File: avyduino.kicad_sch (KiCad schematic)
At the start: 4 parts, among them J1 Power, J2 Digital/PWM, J3 Analog, J4 Digital/PWM

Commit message: make schematic
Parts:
- added C1, C10, C11, C12, C13, C14, C2, C3, C6, C9: 100nF, symbol Device:C
- added C4, C5, C7, C8: 22pF, symbol Device:C
- added D1: D, symbol Device:D
- added FB1: 10uH, symbol Device:FerriteBead
- added J5: USB_C_Receptacle_USB2.0_14P, symbol Connector:USB_C_Receptacle_USB2.0_14P
- added Q1: AO3401A, Package_TO_SOT_SMD:SOT-23, symbol Transistor_FET:AO3401A
- added R1, R5, R6: 10k, symbol Device:R
- added R2: 1m, symbol Device:R
- added R3, R4: 5.1k, symbol Device:R
- added U1: ATmega328P-P, Package_DIP:DIP-28_W7.62mm_Socket_LongPads, symbol MCU_Microchip_ATmega:ATmega328P-P
- added U2: CH340G, Package_SO:SOIC-16_3.9x9.9mm_P1.27mm, symbol Interface_USB:CH340G
- added U3: LM2931AZ-5.0_TO92, Package_TO_SOT_THT:TO-92_Inline, symbol Regulator_Linear:LM2931AZ-5.0_TO92
- added U4: MCP1700x-330xxTT, Package_TO_SOT_SMD:SOT-23, symbol Regulator_Linear:MCP1700x-330xxTT
- added U5: LM358, symbol Amplifier_Operational:LM358
- added Y1: 12MHz, symbol Device:Crystal
- added Y2: 16MHz, symbol Device:Crystal
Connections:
- net IOREF is gone; now on net +5V: J1.2 (Pin_2)
- net *10: now also U1.16 (PB2)
- net *11: now also U1.17 (PB3)
- net *3: now also U1.5 (PD3)
- net *5: now also U1.11 (PD5)
- net *6: now also U1.12 (PD6)
- net *9: now also U1.15 (PB1)
- net +3V3: now also C13.2, U4.2 (VO)
- net +5V: now also C1.1, C11.2, C14.2, FB1.1, Q1.3 (D), R1.1, U1.7 (VCC), U2.16 (VCC), U3.1 (VO), U5.8 (V+)
- net 12: now also U1.18 (PB4)
- net 13: now also U1.19 (PB5)
- net 2: now also U1.4 (PD2)
- net 4: now also U1.6 (PD4)
- net 7: now also U1.13 (PD7)
- net 8: now also U1.14 (PB0)
- net A0: now also U1.23 (PC0)
- net A1: now also U1.24 (PC1)
- net A2: now also U1.25 (PC2)
- net A3: now also U1.26 (PC3)
- net AREF: now also C3.1, U1.21 (AREF)
- net GND: now also C1.2, C10.1, C11.1, C12.1, C13.1, C14.1, C2.2, C3.2, C4.2, C5.2, C7.2, C8.2, C9.2, D1.1 (K), J5.A1 (GND), J5.A12 (GND), J5.B1 (GND), J5.B12 (GND), J5.SH (SHIELD), R3.2, R4.2, R6.2, U1.22 (GND), U1.8 (GND), U2.1 (GND), U3.2 (GND), U4.1 (GND), U5.4 (V-)
- net RX/0: now also U1.2 (PD0), U2.2 (TXD)
- net SCL/A5: now also U1.28 (PC5)
- net SDA/A4: now also U1.27 (PC4)
- net TX/1: now also U1.3 (PD1), U2.3 (RXD)
- net VCC: now also C10.2, C12.2, R5.1, U3.3 (VI), U4.3 (VI)
- net ~{RESET}: now also C6.1, U1.1 (~{RESET}/PC6)
- new net: Q1.1 (G), U5.1
- new net: R5.2, R6.1, U5.2 (-)
- new net: J5.A5 (CC1), R3.1
- new net: C4.1, U2.7 (XI), Y1.1
- new net: C5.1, U2.8 (XO), Y1.2
- new net: C9.1, U2.4 (V3)
- new net: C2.1, FB1.2, U1.20 (AVCC)
- new net: D1.2 (A), R1.2
- new net: J5.B5 (CC2), R4.1
- new net DTR: C6.2, U2.13 (~{DTR})
- new net UD+: J5.A6 (D+), J5.B6 (D+), U2.5 (UD+)
- new net UD-: J5.A7 (D-), J5.B7 (D-), U2.6 (UD-)
- new net VBUS: J5.A4 (VBUS), J5.A9 (VBUS), J5.B4 (VBUS), J5.B9 (VBUS), Q1.2 (S), U5.3 (+)
- new net XTAL1: C8.1, R2.2, U1.9 (XTAL1/PB6), Y2.2
- new net XTAL2: C7.1, R2.1, U1.10 (XTAL2/PB7), Y2.1
- no-connect marks 1 -> 6
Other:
- note added: "3v3 + 5v LDOs"
- note added: "MOSFET for deciding power source"
- note added: "Oscillator for ATmega"
- note added: "Pin Headers"
- note added: "USB to UART"
- note added: "USBC"

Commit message: do layout
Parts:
- removed FB1: 10uH, symbol Device:FerriteBead
- C1, C10, C11, C12, C13, C14, C2, C3, C4, C5, C6, C7, C8, C9: footprint (none) -> Capacitor_SMD:C_0805_2012Metric
- D1: footprint (none) -> Diode_THT:D_DO-35_SOD27_P10.16mm_Horizontal
- J5: footprint (none) -> Connector_USB:USB_C_Receptacle_GCT_USB4105-xx-A_16P_TopMnt_Horizontal
- Q1: MPN (none) -> AO3401A
- R1, R2, R3, R4, R5, R6: footprint (none) -> Resistor_SMD:R_0805_2012Metric
- U1: MPN (none) -> ATmega328P-P
- U2: MPN (none) -> CH340G
- U3: MPN (none) -> LM2931AZ-5.0_TO92
- U4: MPN (none) -> MCP1700x-330xxTT
- U5: footprint (none) -> Package_DIP:DIP-8_W7.62mm_Socket_LongPads; MPN (none) -> LM358
- Y1, Y2: footprint (none) -> Crystal:Crystal_HC49-U_Vertical
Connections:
- net +5V: now also C2.1, U1.20 (AVCC)

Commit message: added icsp header
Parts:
- added J6: ICSP Header, Connector_PinHeader_2.54mm:PinHeader_2x03_P2.54mm_Vertical, symbol Connector_Generic:Conn_02x03_Odd_Even
- added R7: R, Resistor_SMD:R_0805_2012Metric_Pad1.20x1.40mm_HandSolder, symbol Device:R
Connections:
- net *11: now also J6.4 (Pin_4)
- net +5V: now also J6.2 (Pin_2), R7.1
- net 12: now also J6.1 (Pin_1)
- net 13: now also J6.3 (Pin_3)
- net GND: now also J6.6 (Pin_6)
- net ~{RESET}: now also J6.5 (Pin_5), R7.2
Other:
- note added: "ICSP Header"
- moved on the sheet: C1, C2, C3, C6, U1

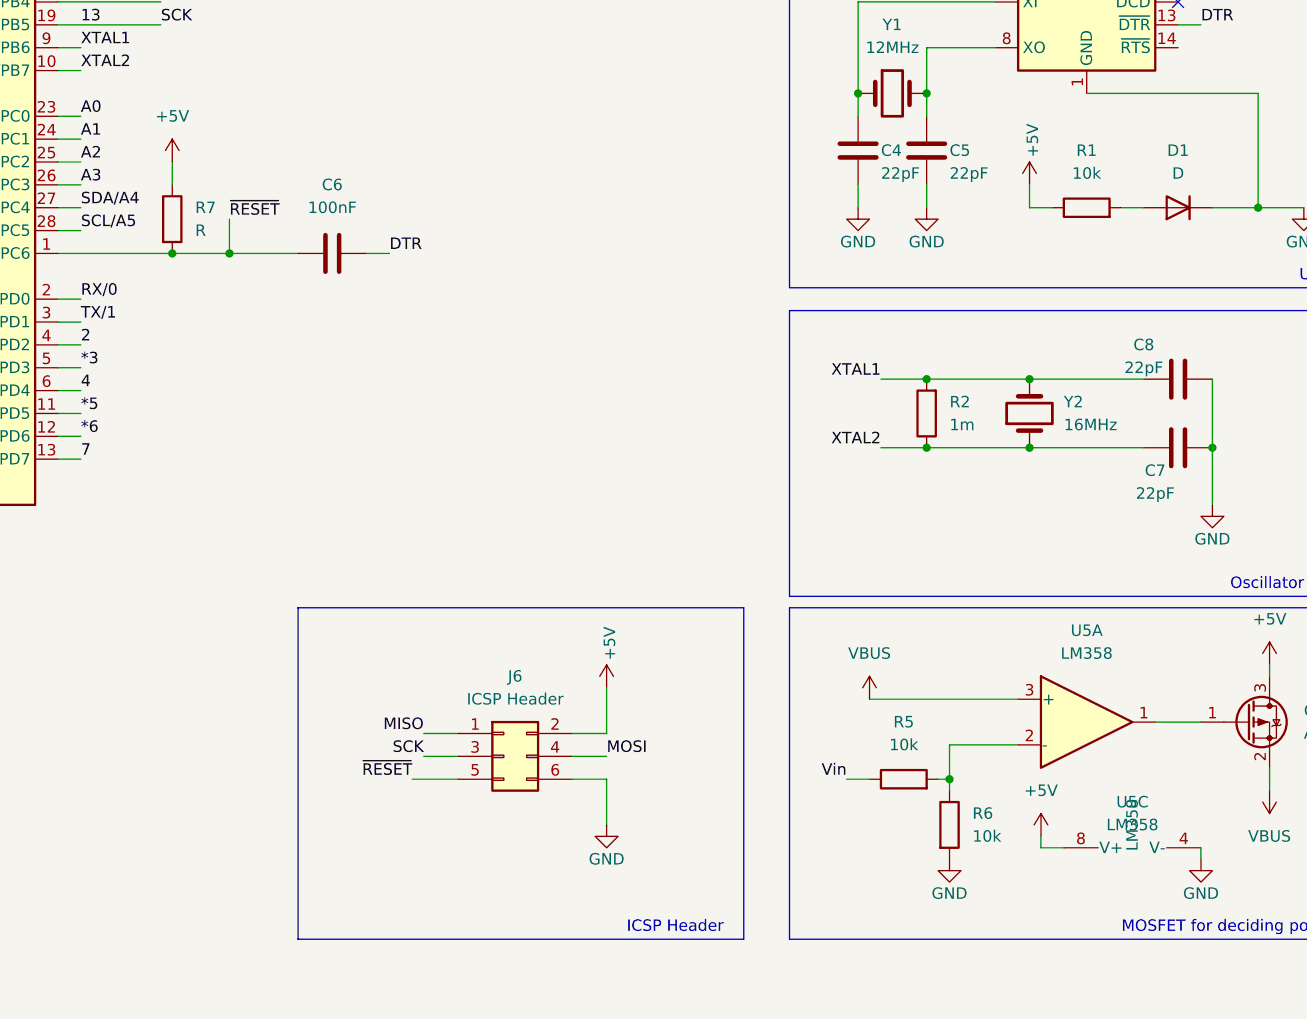
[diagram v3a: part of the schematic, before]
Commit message: routed ICSP header
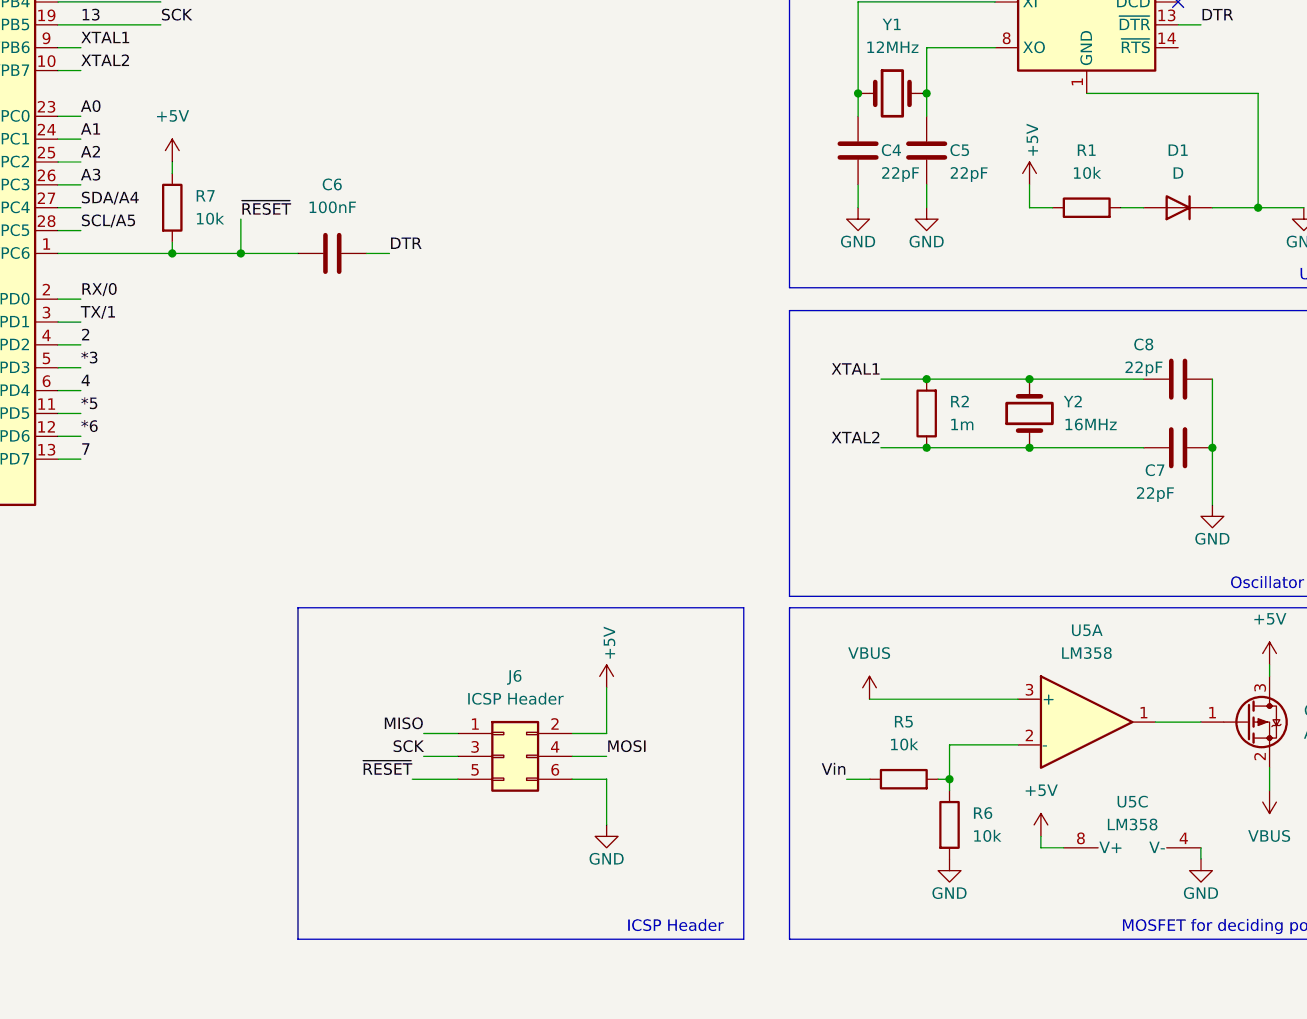
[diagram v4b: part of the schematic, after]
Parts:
- R7: value R -> 10k
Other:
- moved on the sheet: R7
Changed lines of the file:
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@@
 	)
 	(junction
-		(at 148.59 87.63)
-		(diameter 0)
-		(color 0 0 0 0)
-	)
-	(junction
 		(at 226.06 69.85)
 		(diameter 0)
@@
 	)
 	(junction
+		(at 149.86 87.63)
+		(diameter 0)
+		(color 0 0 0 0)
+	)
+	(junction
 		(at 226.06 101.6)
 		(diameter 0)
@@
 	)
 	(junction
+		(at 142.24 87.63)
+		(diameter 0)
+		(color 0 0 0 0)
+	)
+	(junction
 		(at 53.34 96.52)
 		(diameter 0)
@@
 	)
 	(junction
-		(at 142.24 87.63)
-		(diameter 0)
-		(color 0 0 0 0)
-	)
-	(junction
 		(at 241.3 27.9252)
 		(diameter 0)
@@
 	(wire
 		(pts
+			(xy 149.86 87.63) (xy 156.21 87.63)
+		)
+		(stroke
+			(width 0)
+			(type default)
+		)
+	)
+	(wire
+		(pts
 			(xy 226.06 69.85) (xy 226.06 72.39)
 		)
@@
 	(wire
 		(pts
-			(xy 148.59 87.63) (xy 156.21 87.63)
-		)
-		(stroke
-			(width 0)
-			(type default)
-		)
-	)
-	(wire
-		(pts
 			(xy 228.6 146.05) (xy 228.6 147.32)
 		)
@@
 	(wire
 		(pts
-			(xy 142.24 87.63) (xy 148.59 87.63)
-		)
-		(stroke
-			(width 0)
-			(type default)
-		)
-	)
-	(wire
-		(pts
 			(xy 31.75 39.37) (xy 34.29 39.37)
 		)
@@
 	(wire
 		(pts
-			(xy 142.24 77.47) (xy 142.24 80.01)
+			(xy 142.24 77.47) (xy 142.24 78.74)
 		)
 		(stroke
@@
 	(wire
 		(pts
+			(xy 142.24 87.63) (xy 149.86 87.63)
+		)
+		(stroke
+			(width 0)
+			(type default)
+		)
+	)
+	(wire
+		(pts
 			(xy 243.84 31.75) (xy 243.84 39.37)
 		)
@@
 	(wire
 		(pts
+			(xy 142.24 86.36) (xy 142.24 87.63)
+		)
+		(stroke
+			(width 0)
+			(type default)
+		)
+	)
+	(wire
+		(pts
 			(xy 132.08 77.47) (xy 129.54 77.47)
 		)
@@
 	(wire
 		(pts
-			(xy 148.59 83.82) (xy 148.59 87.63)
+			(xy 149.86 83.82) (xy 149.86 87.63)
 		)
 		(stroke
@@
 	)
 	(label "~{RESET}"
-		(at 148.59 83.82 0)
+		(at 149.86 83.82 0)
 		(effects
 			(font
@@
 	(symbol
 		(lib_id "Device:R")
-		(at 142.24 83.82 0)
+		(at 142.24 82.55 0)
 		(unit 1)
 		(body_style 1)
@@
 		(fields_autoplaced yes)
 		(property "Reference" "R7"
-			(at 144.78 82.5499 0)
+			(at 144.78 81.2799 0)
 			(show_name no)
 			(do_not_autoplace no)
@@
 			)
 		)
-		(property "Value" "R"
-			(at 144.78 85.0899 0)
+		(property "Value" "10k"
+			(at 144.78 83.8199 0)
 			(show_name no)
 			(do_not_autoplace no)
@@
 		)
 		(property "Footprint" "Resistor_SMD:R_0805_2012Metric_Pad1.20x1.40mm_HandSolder"
-			(at 140.462 83.82 90)
+			(at 140.462 82.55 90)
 			(hide yes)
 			(show_name no)
@@
 		)
 		(property "Datasheet" ""
-			(at 142.24 83.82 0)
+			(at 142.24 82.55 0)
 			(hide yes)
 			(show_name no)
@@
 		)
 		(property "Description" "Resistor"
-			(at 142.24 83.82 0)
+			(at 142.24 82.55 0)
 			(hide yes)
 			(show_name no)
@@
 			)
 		)
+		(property "MPN" ""
+			(at 142.24 82.55 0)
+			(show_name no)
+			(do_not_autoplace no)
+			(effects
+				(font
+					(size 1.27 1.27)
+				)
+			)
+		)
 		(pin "1"
 		)
@@
 		(property "MPN" "LM358"
 			(at 248.92 151.13 0)
+			(hide yes)
 			(show_name no)
 			(do_not_autoplace no)

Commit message: redo layout of pcb
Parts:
- removed U4: MCP1700x-330xxTT, Package_TO_SOT_SMD:SOT-23, symbol Regulator_Linear:MCP1700x-330xxTT
- added U4: MCP1700x-330xxTO, Package_TO_SOT_THT:TO-92_Inline, symbol Regulator_Linear:MCP1700x-330xxTO
- C1, C10, C11, C12, C13, C14, C2, C3, C6, C9: MPN (none) -> C0805C104K5RACTU
- C4, C5, C7, C8: MPN (none) -> C0805C220J5GACTU
- D1: value D -> Diode; MPN (none) -> 1N4148
- J1: value Power -> Power Header; MPN (none) -> SSW-108-01-T-S
- J2: value Digital/PWM -> Digital/PWM Header; MPN (none) -> SSW-110-01-T-S
- J3: value Analog -> Analog Header; MPN (none) -> SSW-106-01-T-S
- J4: value Digital/PWM -> Digital/PWM Header; MPN (none) -> SSW-108-01-T-S
- J5: MPN (none) -> SS-52400-002
- J6: MPN (none) -> TSW-103-07-G-D
- R1, R5, R6, R7: MPN (none) -> ERJ6ENF1002V
- R2: MPN (none) -> EE-SX953-W 1M
- R3, R4: MPN (none) -> RC0805FR-075K1L
- U1: MPN ATmega328P-P -> ATMEGA328P-PU
- U3: MPN LM2931AZ-5.0_TO92 -> LM2931AZ-5.0RAG
- U5: MPN LM358 -> LM358S-13
- Y1: MPN (none) -> ABLS2-12.000MHZ-D4Y-T
- Y2: MPN (none) -> ABM8G-16.000MHZ-18-D2Y-T
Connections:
- net +3V3: now also U4.2 (VI)
- net GND: now also U4.1 (GND)
- net VCC: now also U4.3 (VO)

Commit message: route pcb and make BOMs
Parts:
- R2: MPN EE-SX953-W 1M -> AC0805FR-071ML
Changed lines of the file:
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@@
 			)
 		)
-		(property "MPN" "EE-SX953-W 1M"
+		(property "MPN" "AC0805FR-071ML"
 			(at 226.06 105.41 0)
 			(hide yes)

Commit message: redo layout and add reset button
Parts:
- added SW1: ~{RESET}, Button_Switch_THT:SW_PUSH_6mm, symbol Switch:SW_Push
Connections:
- net GND: now also SW1.2
- net ~{RESET}: now also SW1.1
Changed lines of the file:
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@@
 	(wire
 		(pts
+			(xy 187.96 114.3) (xy 187.96 110.49)
+		)
+		(stroke
+			(width 0)
+			(type default)
+		)
+	)
+	(wire
+		(pts
 			(xy 53.34 96.52) (xy 53.34 102.87)
 		)
@@
 	(wire
 		(pts
+			(xy 168.91 110.49) (xy 176.53 110.49)
+		)
+		(stroke
+			(width 0)
+			(type default)
+		)
+	)
+	(wire
+		(pts
 			(xy 93.98 180.34) (xy 82.55 180.34)
 		)
@@
 	(wire
 		(pts
+			(xy 187.96 110.49) (xy 186.69 110.49)
+		)
+		(stroke
+			(width 0)
+			(type default)
+		)
+	)
+	(wire
+		(pts
 			(xy 132.08 49.53) (xy 129.54 49.53)
 		)
@@
 		)
 	)
+	(label "~{RESET}"
+		(at 168.91 110.49 180)
+		(effects
+			(font
+				(size 1.27 1.27)
+			)
+			(justify right bottom)
+		)
+	)
 	(label "SCK"
 		(at 140.97 62.23 0)
@@
 	)
 	(symbol
+		(lib_id "power:GND")
+		(at 187.96 114.3 0)
+		(unit 1)
+		(body_style 1)
+		(exclude_from_sim no)
+		(in_bom yes)
+		(on_board yes)
+		(in_pos_files yes)
+		(dnp no)
+		(property "Reference" "#PWR034"
+			(at 187.96 120.65 0)
+			(hide yes)
+			(show_name no)
+			(do_not_autoplace no)
+			(effects
+				(font
+					(size 1.27 1.27)
+				)
+			)
+		)
+		(property "Value" "GND"
+			(at 187.96 118.11 0)
+			(show_name no)
+			(do_not_autoplace no)
+			(effects
+				(font
+					(size 1.27 1.27)
+				)
+			)
+		)
+		(property "Footprint" ""
+			(at 187.96 114.3 0)
+			(show_name no)
+			(do_not_autoplace no)
+			(effects
+				(font
+					(size 1.27 1.27)
+				)
+			)
+		)
+		(property "Datasheet" ""
+			(at 187.96 114.3 0)
+			(show_name no)
+			(do_not_autoplace no)
+			(effects
+				(font
+					(size 1.27 1.27)
+				)
+			)
+		)
+		(property "Description" "Power symbol creates a global label with name \"GND\" , ground"
+			(at 187.96 114.3 0)
+			(hide yes)
+			(show_name no)
+			(do_not_autoplace no)
+			(effects
+				(font
+					(size 1.27 1.27)
+				)
+			)
+		)
+		(pin "1"
+		)
+		(instances
+			(project "avyduino"
+				(path "/e63e39d7-6ac0-4ffd-8aa3-1841a4541b55"
+					(reference "#PWR034")
+					(unit 1)
+				)
+			)
+		)
+	)
+	(symbol
 		(lib_id "Device:R")
 		(at 60.96 110.49 90)
@@
 					(unit 1)
 				)
+			)
+		)
+	)
+	(symbol
+		(lib_id "Switch:SW_Push")
+		(at 181.61 110.49 0)
+		(unit 1)
+		(body_style 1)
+		(exclude_from_sim no)
+		(in_bom yes)
+		(on_board yes)
+		(in_pos_files yes)
+		(dnp no)
+		(fields_autoplaced yes)
+		(property "Reference" "SW1"
+			(at 181.61 102.87 0)
+			(show_name no)
+			(do_not_autoplace no)
+			(effects
+				(font
+					(size 1.27 1.27)
+				)
+			)
+		)
+		(property "Value" "~{RESET}"
+			(at 181.61 105.41 0)
+			(show_name no)
+			(do_not_autoplace no)
+			(effects
+				(font
+					(size 1.27 1.27)
+				)
+			)
+		)
+		(property "Footprint" "Button_Switch_THT:SW_PUSH_6mm"
+			(at 181.61 105.41 0)
+			(hide yes)
+			(show_name no)
+			(do_not_autoplace no)
+			(effects
+				(font
+					(size 1.27 1.27)
+				)
+			)
+		)
+		(property "Datasheet" ""
+			(at 181.61 105.41 0)
+			(hide yes)
+			(show_name no)
+			(do_not_autoplace no)
+			(effects
+				(font
+					(size 1.27 1.27)
+				)
+			)
+		)
+		(property "Description" "Push button switch, generic, two pins"
+			(at 181.61 110.49 0)
+			(hide yes)
+			(show_name no)
+			(do_not_autoplace no)
+			(effects
+				(font
+					(size 1.27 1.27)
+				)
+			)
+		)
+		(property "MPN" ""
+			(at 181.61 110.49 0)
+			(show_name no)
+			(do_not_autoplace no)
+			(effects
+				(font
+					(size 1.27 1.27)
+				)
+			)
+		)
+		(pin "1"
+		)
+		(pin "2"
+		)
+		(instances
+			(project "avyduino"
+				(path "/e63e39d7-6ac0-4ffd-8aa3-1841a4541b55"
+					(reference "SW1")
+					(unit 1)
+				)
